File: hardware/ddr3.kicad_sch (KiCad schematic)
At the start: 24 parts, among them U2 H5TQ4G63EFR

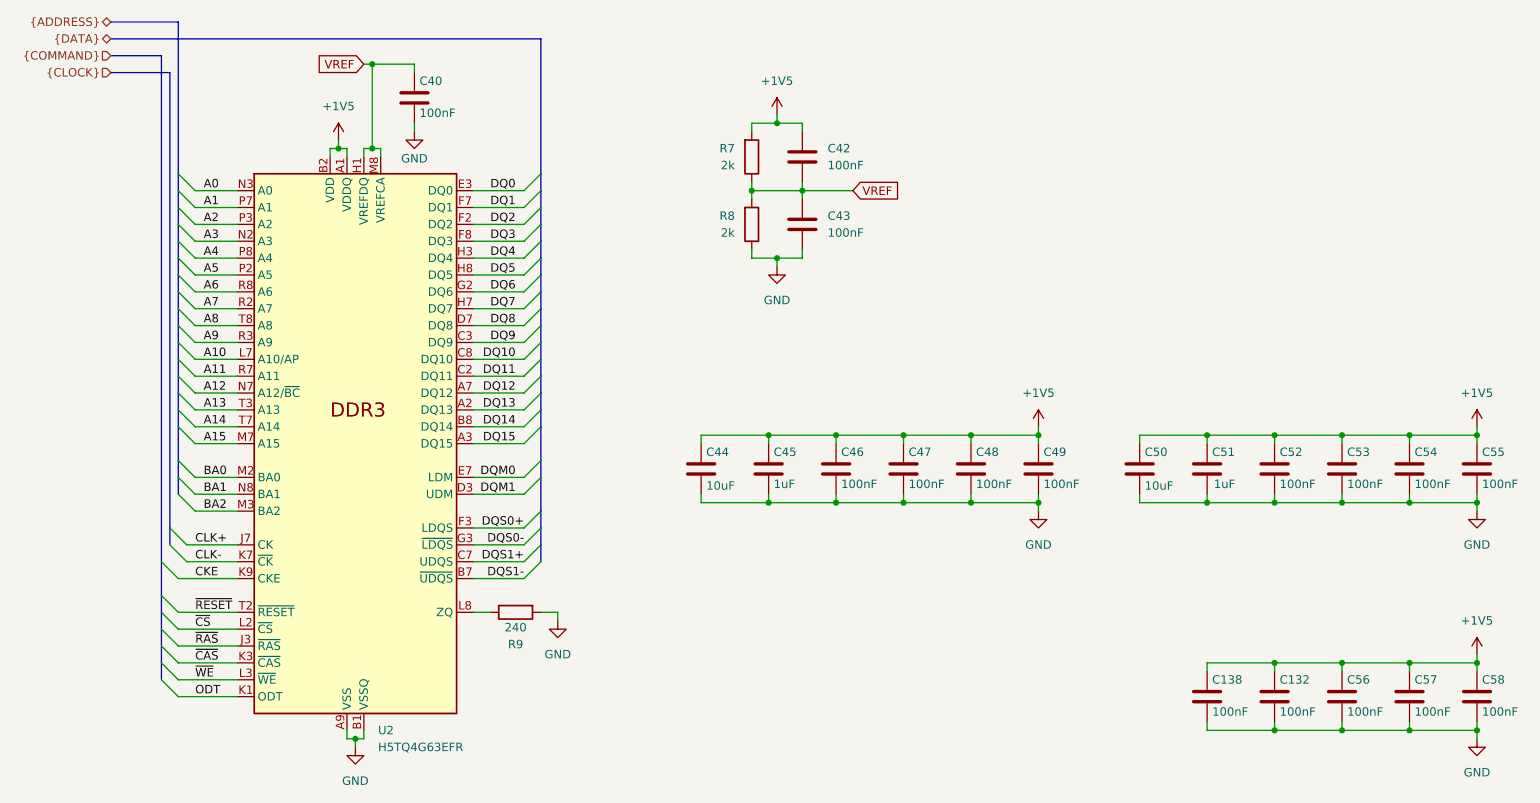
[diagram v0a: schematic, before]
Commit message: Update crystal
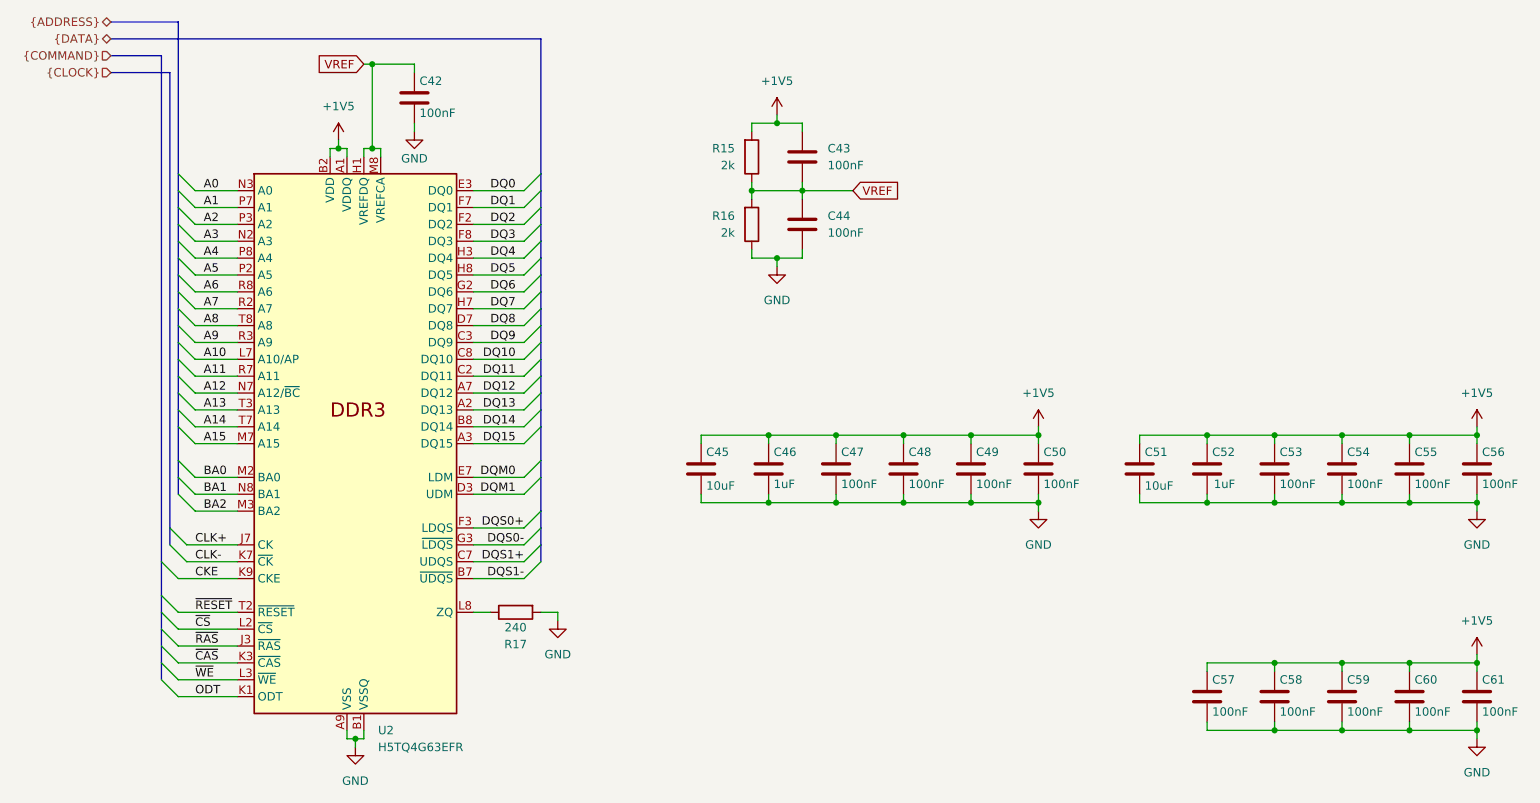
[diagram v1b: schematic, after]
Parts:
- renumbered C40 to C42, C42 to C43, C43 to C44, C44 to C45, C45 to C46, C46 to C47, C47 to C48, C48 to C49, C49 to C50, C50 to C51, C51 to C52, C52 to C53, C53 to C54, C54 to C55, C55 to C56, C138 to C57, C132 to C58, C56 to C59, C57 to C60, C58 to C61, R7 to R15, R8 to R16, R9 to R17

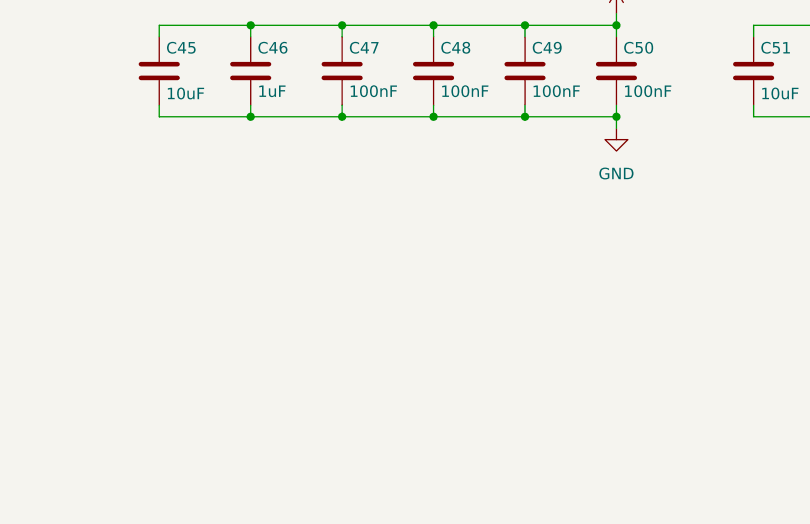
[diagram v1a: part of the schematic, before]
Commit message: Changed crystal and fix USB data lines
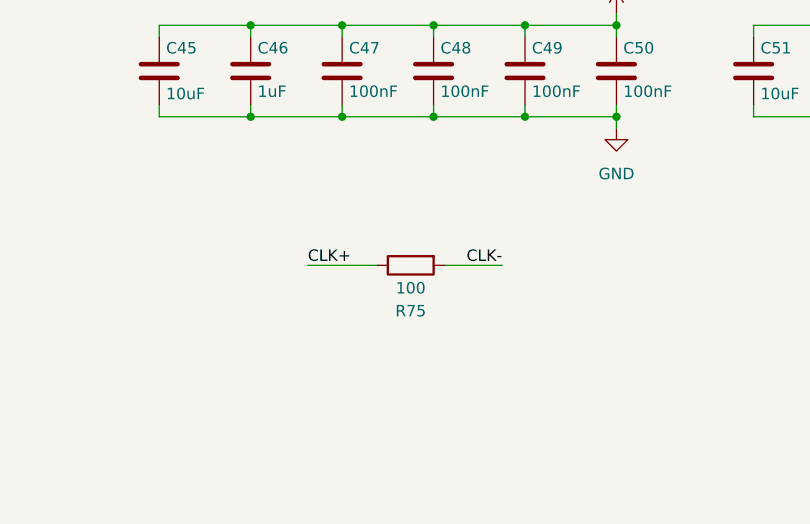
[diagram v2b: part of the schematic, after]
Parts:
- added R75: 100, Resistor_SMD:R_0402_1005Metric, symbol Device:R
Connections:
- net CLK+: now also R75.1
- net CLK-: now also R75.2
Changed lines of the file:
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@@
 		)
 	)
+	(wire
+		(pts
+			(xy 163.83 134.62) (xy 171.45 134.62)
+		)
+		(stroke
+			(width 0)
+			(type default)
+		)
+	)
 	(bus
 		(pts
@@
 	(wire
 		(pts
+			(xy 179.07 134.62) (xy 185.42 134.62)
+		)
+		(stroke
+			(width 0)
+			(type default)
+		)
+	)
+	(wire
+		(pts
 			(xy 254 107.95) (xy 243.84 107.95)
 		)
@@
 		)
 	)
+	(label "CLK-"
+		(at 185.42 134.62 180)
+		(effects
+			(font
+				(size 1.27 1.27)
+			)
+			(justify right bottom)
+		)
+	)
 	(label "DQS1-"
 		(at 120.65 129.54 180)
@@
 		)
 	)
+	(label "CLK+"
+		(at 163.83 134.62 0)
+		(effects
+			(font
+				(size 1.27 1.27)
+			)
+			(justify left bottom)
+		)
+	)
 	(label "DQ6"
 		(at 119.38 86.36 180)
@@
 					(unit 1)
 				)
+			)
+		)
+	)
+	(symbol
+		(lib_id "Device:R")
+		(at 175.26 134.62 90)
+		(mirror x)
+		(unit 1)
+		(exclude_from_sim no)
+		(in_bom yes)
+		(on_board yes)
+		(dnp no)
+		(property "Reference" "R75"
+			(at 175.26 139.7 90)
+			(effects
+				(font
+					(size 1.27 1.27)
+				)
+			)
+		)
+		(property "Value" "100"
+			(at 175.26 137.16 90)
+			(effects
+				(font
+					(size 1.27 1.27)
+				)
+			)
+		)
+		(property "Footprint" "Resistor_SMD:R_0402_1005Metric"
+			(at 175.26 132.842 90)
+			(effects
+				(font
+					(size 1.27 1.27)
+				)
+				(hide yes)
+			)
+		)
+		(property "Datasheet" "~"
+			(at 175.26 134.62 0)
+			(effects
+				(font
+					(size 1.27 1.27)
+				)
+				(hide yes)
+			)
+		)
+		(property "Description" "Resistor"
+			(at 175.26 134.62 0)
+			(effects
+				(font
+					(size 1.27 1.27)
+				)
+				(hide yes)
+			)
+		)
+		(pin "1"
+		)
+		(pin "2"
+		)
+		(instances
+			(project ""
+				(path "/b53f5dbb-8078-4818-9e8f-fdf90ba6d854/32a4bb18-2695-4537-bbd4-f872ec13cb53"
+					(reference "R75")
+					(unit 1)
+				)

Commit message: Add schematic pdf
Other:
- title: Icepi CM0 -> Icepi SBC
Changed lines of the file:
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@@
 	(paper "A4")
 	(title_block
-		(title "Icepi CM0")
-		(date "2025-11-21")
+		(title "Icepi SBC")
+		(date "2025-12-21")
 		(rev "v1.0")
 		(company "Icy Electronics")
 		(comment 1 "Chengyin Yao (cheyao)")
-		(comment 2 "https://github.com/cheyao/icepi-cm0")
+		(comment 2 "https://github.com/cheyao/icepi-sbc")
 		(comment 3 "License: Solderpad")
 	)
@@
 	)
 	(image
-		(at 232.156 59.69)
+		(at 234.442 52.07)
 		(data "iVBORw0KGgoAAAANSUhEUgAAAwoAAAMyCAIAAABCc6G2AAAAA3NCSVQICAjb4U/gAAAgAElEQVR4"
 			"nOy9Z7hlVZk1Ot4ZVtjxpMqZqoIiJymiKGVJ1kYQtM2CCKgYultbbXPbJtRW8VNQGkliwCwKSM5I"
